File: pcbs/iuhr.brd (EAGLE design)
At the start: 38.4 x 23 mm, 81 parts, among them Q1 20.000MHz, Q2 MOSFET-NCHANNELSMD

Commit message: correct power-on button and add detection
ToDo: - reassign DIGIT6
      - layout for this commit
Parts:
- added 12V_IN1: TPTP20SQ, testpad:TP20SQ
- added D1: (no value), diode:SOD323-R
- R12: value 100 -> 14k
- moved R12 40.2 mm to (0.60, -14.4), flipped to the top, turned to 0 degrees
- renumbered ONBTN to ONBTN_B, ONBTN_3V3 to ONBTN_A
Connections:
- new net N$63: 12V_IN1.TP, R12.2
- new net N$64: ATMEGA88PA.11, D1.A
- net DIGIT6: no longer ATMEGA88PA.19
- net N$59: now also ONBTN_A.TP, R12.1; no longer ONBTN_B.TP, R12.2
- net ON: now also ATMEGA88PA.19, D1.C, ONBTN_B.TP; no longer ATMEGA88PA.11, R12.1
- net VCC: no longer ONBTN_A.TP
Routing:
- net VCC: track 69.6 -> 64.2 mm
- net N$59: track 3.52 -> 0.00 mm
- net ON: track 23.9 -> 21.8 mm
- net DIGIT6: track 4.30 -> 3.40 mm

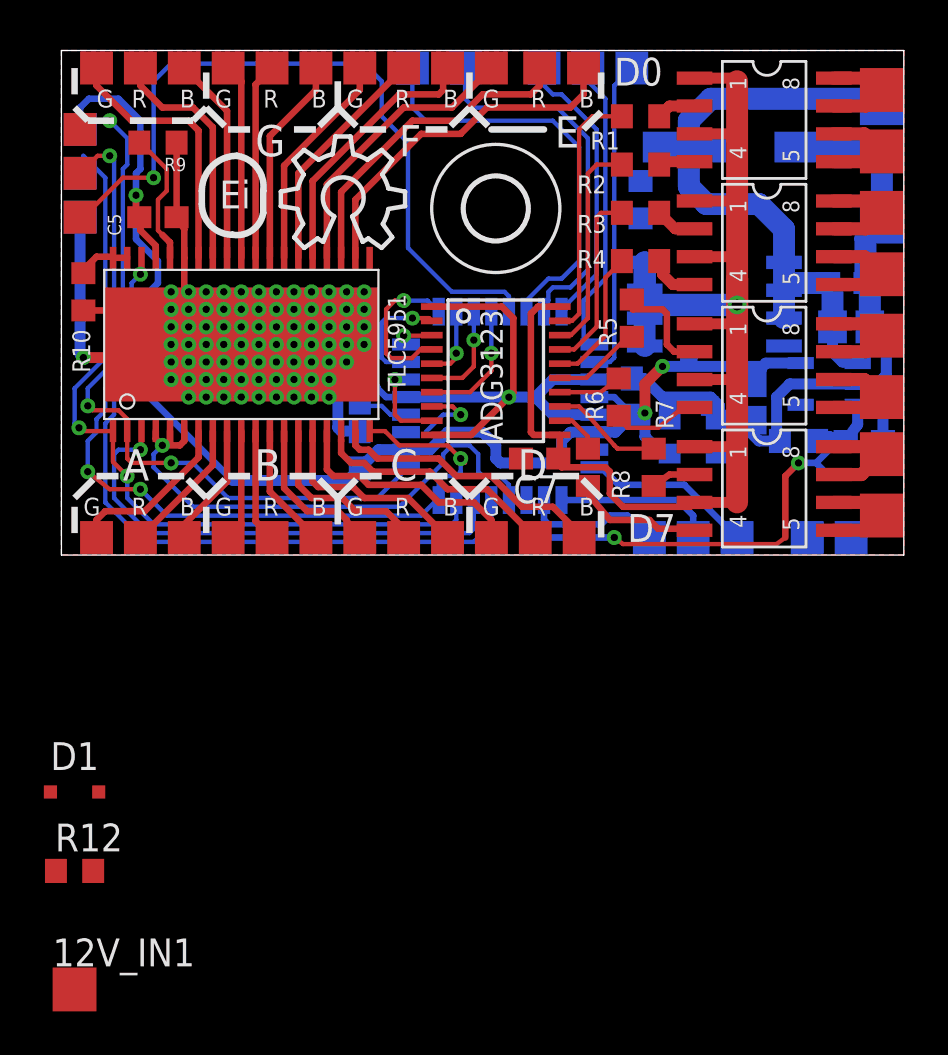
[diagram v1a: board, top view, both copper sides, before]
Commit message: Can now use "ON" Switch to turn board off
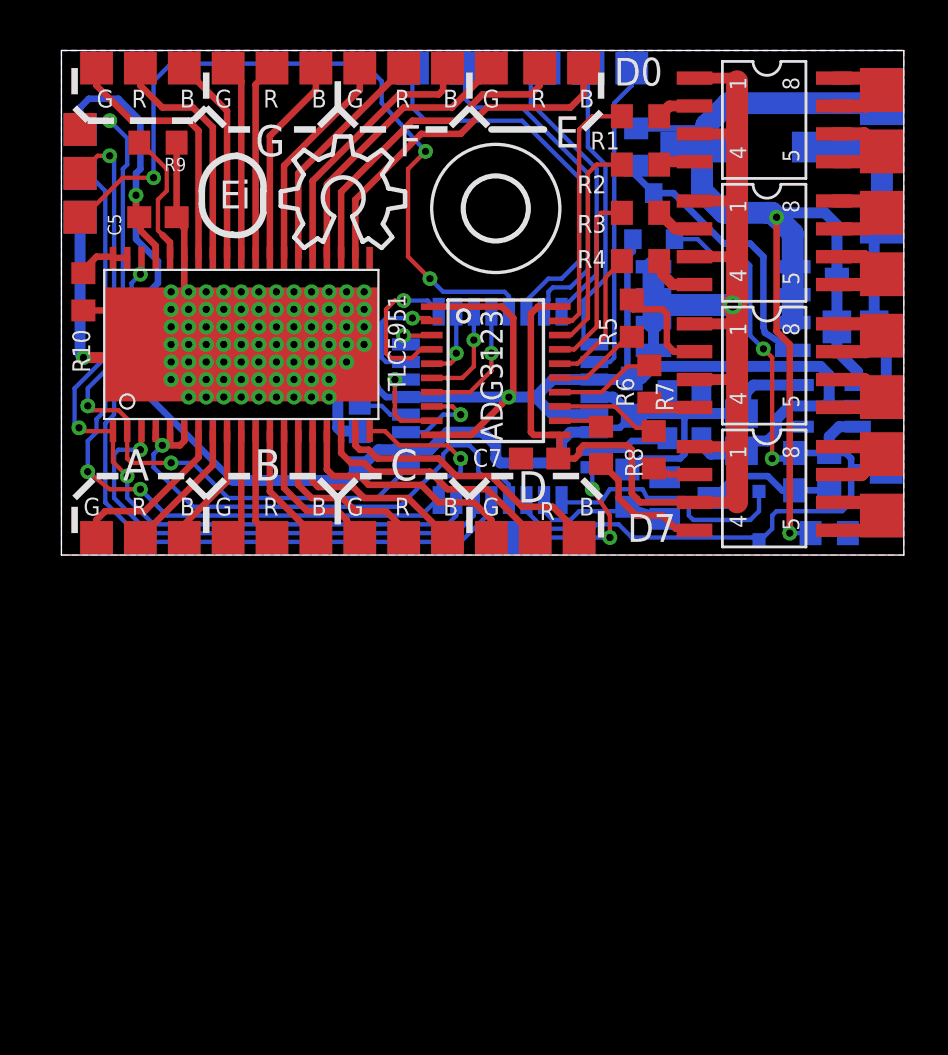
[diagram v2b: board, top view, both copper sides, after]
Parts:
- removed 12V_IN1: TPTP20SQ, testpad:TP20SQ
- removed PD5, PD6: TPTP15SQ, testpad:TP15SQ
- removed U$2: IRF7416, ShortCircuitRobotics:SO8-2
- added D2: 4.7V, diode:SOT23
- added IRF7416: IRF7416, ShortCircuitRobotics:SO8-2
- added R14: 300, resistor:R0603
- moved R12 37.7 mm to (35.0, 1.00), flipped to the bottom
- moved D1 33.6 mm to (31.8, 1.80), flipped to the bottom, turned to 90 degrees
- moved PB7 10.4 mm to (20.4, 0.80)
- moved Q2 7.77 mm to (27.0, 15.4)
- moved ONBTN_A 3.69 mm to (37.6, 1.60), turned to 270 degrees
- moved ONBTN_B 3.58 mm to (37.6, 4.00)
- moved C8 3.49 mm to (33.4, 3.80), turned to 270 degrees
- moved R13 2.41 mm to (26.2, 18.6)
- moved R11 1.98 mm to (35.0, 3.80), turned to 90 degrees
- moved R6 1.52 mm to (26.8, 7.80)
- moved C6 1.46 mm to (31.0, 5.60)
- moved R8 1.17 mm to (24.6, 5.00)
- moved Q1 1.08 mm to (28.4, 6.40), turned to 270 degrees
- moved TPS70933 1.00 mm to (35.0, 6.80)
- moved C13 0.80 mm to (32.2, 18.6)
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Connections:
- removed net N$63: 12V_IN1.TP, R12.2
- removed net N$64: ATMEGA88PA.11, D1.A
- net +12V: now also IRF7416.1, IRF7416.2, IRF7416.3, R12.2; no longer U$2.1, U$2.2, U$2.3
- net DIGIT6: now also ATMEGA88PA.19
- net GND: now also D2.3
- net N$56: now also D1.A; no longer PD5.TP
- net N$57: now also D2.1, R14.1; no longer PD6.TP
- net N$61: now also IRF7416.4; no longer U$2.4
- net ON: now also ATMEGA88PA.11; no longer ATMEGA88PA.19
- net VCC: now also R14.2
- net VPP: now also IRF7416.5, IRF7416.6, IRF7416.7, IRF7416.8; no longer U$2.5, U$2.6, U$2.7, U$2.8
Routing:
- net +12V: track 29.9 -> 50.4 mm, vias 0 -> 2
- net ON: track 21.8 -> 40.1 mm
- net GND: track 103.9 -> 119.9 mm
- net N$61: track 0.00 -> 12.8 mm
- net N$56: track 7.29 -> 12.2 mm
- net CLK_STM: track 0.00 -> 3.55 mm
- net N$44: track 4.11 -> 2.15 mm
- net N$59: track 0.00 -> 1.93 mm
- net N$46: track 2.89 -> 4.59 mm
- net MOSI: track 35.7 -> 34.4 mm
- net VCC: track 64.2 -> 65.3 mm, vias 3 -> 1
- net N$12: track 17.0 -> 16.0 mm
- net N$58: track 7.83 -> 8.76 mm, vias 0 -> 2
- net DIGIT6: track 3.40 -> 4.30 mm
- net RESET: track 34.6 -> 35.5 mm, vias 1 -> 3
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- added copper zone on layer 16, net GND

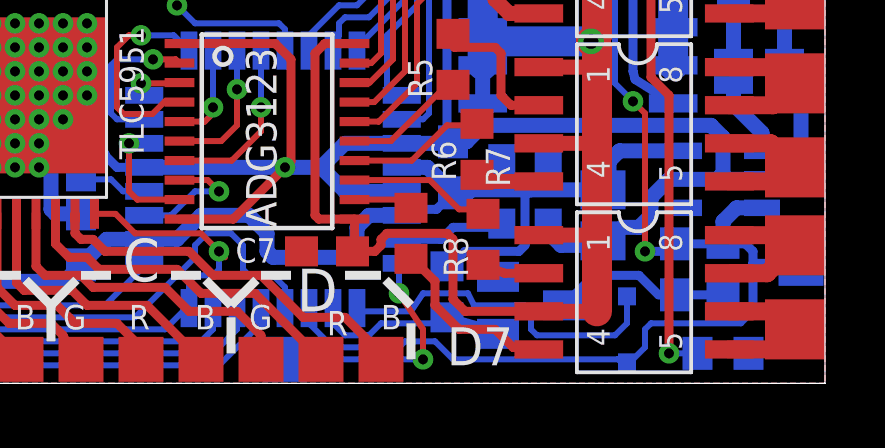
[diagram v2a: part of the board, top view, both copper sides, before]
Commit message: Swap functionality of PB7 and PD5
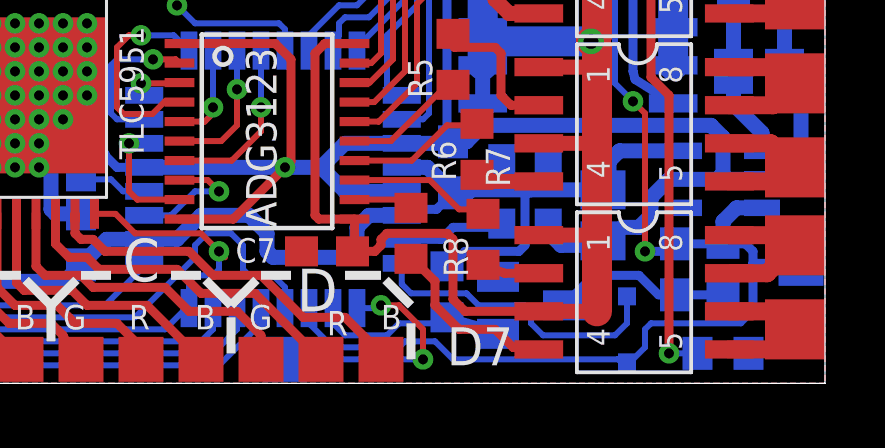
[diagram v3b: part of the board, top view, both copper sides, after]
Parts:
- renumbered PB7 to PD5
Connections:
- net N$56: now also PD5.TP; no longer D1.A
- net N$58: now also D1.A; no longer PD5.TP
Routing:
- net N$56: track 12.2 -> 8.17 mm, vias 0 -> 2
- net N$58: track 8.76 -> 10.3 mm, vias 2 -> 0
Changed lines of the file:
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@@
 <grid distance="0.2" unitdist="mm" unit="mm" style="dots" multiple="1" display="yes" altdistance="0.15875" altunitdist="mm" altunit="mm"/>
 <layers>
-<layer number="1" name="Top" color="4" fill="1" visible="no" active="yes"/>
+<layer number="1" name="Top" color="4" fill="1" visible="yes" active="yes"/>
 <layer number="2" name="Route2" color="1" fill="3" visible="no" active="no"/>
 <layer number="3" name="Route3" color="4" fill="3" visible="no" active="no"/>
@@
 <layer number="19" name="Unrouted" color="6" fill="1" visible="yes" active="yes"/>
 <layer number="20" name="Dimension" color="15" fill="1" visible="yes" active="yes"/>
-<layer number="21" name="tPlace" color="7" fill="1" visible="no" active="yes"/>
+<layer number="21" name="tPlace" color="7" fill="1" visible="yes" active="yes"/>
 <layer number="22" name="bPlace" color="7" fill="1" visible="yes" active="yes"/>
-<layer number="23" name="tOrigins" color="15" fill="1" visible="no" active="yes"/>
+<layer number="23" name="tOrigins" color="15" fill="1" visible="yes" active="yes"/>
 <layer number="24" name="bOrigins" color="15" fill="1" visible="yes" active="yes"/>
-<layer number="25" name="tNames" color="7" fill="1" visible="no" active="yes"/>
+<layer number="25" name="tNames" color="7" fill="1" visible="yes" active="yes"/>
 <layer number="26" name="bNames" color="7" fill="1" visible="yes" active="yes"/>
 <layer number="27" name="tValues" color="7" fill="1" visible="no" active="yes"/>
@@
 <layer number="37" name="tTest" color="7" fill="1" visible="no" active="yes"/>
 <layer number="38" name="bTest" color="7" fill="1" visible="no" active="yes"/>
-<layer number="39" name="tKeepout" color="4" fill="11" visible="no" active="yes"/>
+<layer number="39" name="tKeepout" color="4" fill="11" visible="yes" active="yes"/>
 <layer number="40" name="bKeepout" color="1" fill="11" visible="yes" active="yes"/>
 <layer number="41" name="tRestrict" color="4" fill="10" visible="no" active="yes"/>
@@
 <layer number="49" name="Reference" color="7" fill="1" visible="no" active="yes"/>
 <layer number="50" name="dxf" color="7" fill="1" visible="no" active="no"/>
-<layer number="51" name="tDocu" color="7" fill="1" visible="no" active="yes"/>
+<layer number="51" name="tDocu" color="7" fill="1" visible="yes" active="yes"/>
 <layer number="52" name="bDocu" color="7" fill="1" visible="yes" active="yes"/>
 <layer number="53" name="tGND_GNDA" color="7" fill="9" visible="no" active="no"/>
@@
 <element name="H2" library="holes" package="2,8" value="MOUNT-HOLE2.8" x="19.8" y="15.8"/>
 <element name="LOGO1" library="ea" package="OSHW_8X200_NOTEXT" value="OSHW_LOGO_8MILX0200-NT" x="10" y="14"/>
-<element name="PB7" library="testpad" package="TP15SQ" value="TPTP15SQ" x="20.4" y="0.8" smashed="yes" rot="MR0">
+<element name="PD5" library="testpad" package="TP15SQ" value="TPTP15SQ" x="20.4" y="0.8" smashed="yes" rot="MR0">
 <attribute name="TP_SIGNAL_NAME" value="" x="20.4" y="-1.74" size="1" layer="38" rot="MR0"/>
 <attribute name="NAME" x="20.7501" y="4.0001" size="0.8128" layer="26" rot="MR270"/>
@@
 <signal name="N$58">
 <contactref element="ATMEGA88PA" pad="8"/>
-<contactref element="PB7" pad="TP"/>
-<wire x1="20.4" y1="0.8" x2="20.8" y2="0.8" width="0.2" layer="16"/>
-<wire x1="20.8" y1="0.8" x2="21" y2="0.6" width="0.2" layer="16"/>
-<via x="25" y="0.8" extent="1-16" drill="0.3302"/>
-<wire x1="25" y1="0.8" x2="25" y2="1.8" width="0.2" layer="1"/>
-<wire x1="25" y1="1.8" x2="24.2" y2="3" width="0.2" layer="1"/>
-<via x="24.2" y="3" extent="1-16" drill="0.3302"/>
-<wire x1="24.2" y1="3" x2="24.2" y2="3.9074" width="0.2" layer="16"/>
 <wire x1="24.2" y1="3.9074" x2="24.2926" y2="4" width="0.2" layer="16"/>
-<wire x1="25" y1="0.8" x2="20.4" y2="0.8" width="0.2" layer="16"/>
+<contactref element="D1" pad="A"/>
+<wire x1="24.2926" y1="4" x2="24.2926" y2="3.3074" width="0.2" layer="16"/>
+<wire x1="24.2926" y1="3.3074" x2="24.6" y2="3" width="0.2" layer="16"/>
+<wire x1="24.6" y1="3" x2="26.45" y2="3" width="0.2" layer="16"/>
+<wire x1="26.45" y1="3" x2="26.85" y2="2.6" width="0.2" layer="16"/>
+<wire x1="26.85" y1="2.6" x2="28.4" y2="2.6" width="0.2" layer="16"/>
+<wire x1="28.4" y1="2.6" x2="28.6" y2="2.4" width="0.2" layer="16"/>
+<wire x1="28.6" y1="2.4" x2="28.6" y2="2" width="0.2" layer="16"/>
+<wire x1="28.6" y1="2" x2="29" y2="1.6" width="0.2" layer="16"/>
+<wire x1="29" y1="1.6" x2="31.4" y2="1.6" width="0.2" layer="16"/>
+<wire x1="31.4" y1="1.6" x2="31.8" y2="2" width="0.2" layer="16"/>
+<wire x1="31.8" y1="2" x2="31.8" y2="2.9" width="0.2" layer="16"/>
 </signal>
 <signal name="VPP">
@@
 <wire x1="37.2" y1="1.2" x2="37.6" y2="1.6" width="0.3" layer="16"/>
 </signal>
-<signal name="N$56">
-<contactref element="ATMEGA88PA" pad="9"/>
-<contactref element="D1" pad="A"/>
-<wire x1="28.4" y1="2.6" x2="28.6" y2="2.4" width="0.2" layer="16"/>
-<wire x1="28.6" y1="2.4" x2="28.6" y2="1.8" width="0.2" layer="16"/>
-<wire x1="28.6" y1="1.8" x2="28.8" y2="1.6" width="0.2" layer="16"/>
-<wire x1="28.8" y1="1.6" x2="31.4" y2="1.6" width="0.2" layer="16"/>
-<wire x1="31.4" y1="1.6" x2="31.8" y2="2" width="0.2" layer="16"/>
-<wire x1="31.8" y1="2" x2="31.8" y2="2.9" width="0.2" layer="16"/>
-<wire x1="22.8926" y1="2.6" x2="22.8926" y2="2.3074" width="0.2" layer="16"/>
-<wire x1="22.8" y1="2.5074" x2="22.8926" y2="2.6" width="0.3" layer="16"/>
-<wire x1="25" y1="3" x2="26.5" y2="3" width="0.2" layer="16"/>
-<wire x1="26.7" y1="2.6" x2="28.4" y2="2.6" width="0.2" layer="16"/>
-<wire x1="22.8926" y1="2.1074" x2="22.8926" y2="2.3074" width="0.2" layer="16"/>
-<wire x1="22.8926" y1="2.3074" x2="22.8" y2="2.4" width="0.2" layer="16"/>
-<wire x1="22.8" y1="2.4" x2="24.6" y2="2.4" width="0.2" layer="16"/>
-<wire x1="24.6" y1="2.4" x2="25" y2="3" width="0.2" layer="16"/>
-<wire x1="26.5" y1="3" x2="26.7" y2="2.6" width="0.2" layer="16"/>
-</signal>
 <signal name="N$57">
 <contactref element="D2" pad="1"/>
@@
 <wire x1="25.8" y1="2.2" x2="27.4" y2="1.75" width="0.3" layer="16"/>
 <wire x1="27.4" y1="1.75" x2="27.5" y2="1.65" width="0.3" layer="16"/>
-<wire x1="22.4" y1="1.6" x2="23.2" y2="1.6" width="0.2" layer="16"/>
-<wire x1="23.2" y1="1.6" x2="23.6" y2="2" width="0.2" layer="16"/>
-<wire x1="23.6" y1="2" x2="25.65" y2="2" width="0.2" layer="16"/>
+<wire x1="22.4" y1="1.6" x2="23.8" y2="1.6" width="0.2" layer="16"/>
+<wire x1="23.8" y1="1.6" x2="24.2" y2="2" width="0.2" layer="16"/>
+<wire x1="24.2" y1="2" x2="25.65" y2="2" width="0.2" layer="16"/>
 <wire x1="25.65" y1="2" x2="25.8" y2="2.2" width="0.2" layer="16"/>
 </signal>
+<signal name="N$56">
+<contactref element="ATMEGA88PA" pad="9"/>
+<contactref element="PD5" pad="TP"/>
+<wire x1="20.4" y1="0.8" x2="25" y2="0.8" width="0.2" layer="16"/>
+<wire x1="25" y1="0.8" x2="25" y2="1.8" width="0.2" layer="1"/>
+<wire x1="25" y1="1.8" x2="24.2" y2="2.6" width="0.2" layer="1"/>
+<wire x1="24.2" y1="2.6" x2="23.6" y2="2.6" width="0.2" layer="1"/>
+<wire x1="23.6" y1="2.6" x2="23.5074" y2="2.5074" width="0.2" layer="16"/>
+<wire x1="23.5074" y1="2.5074" x2="22.8" y2="2.5074" width="0.2" layer="16"/>
+<via x="23.6" y="2.6" extent="1-16" drill="0.332"/>
+<via x="25" y="0.8" extent="1-16" drill="0.332"/>
+</signal>
 </signals>

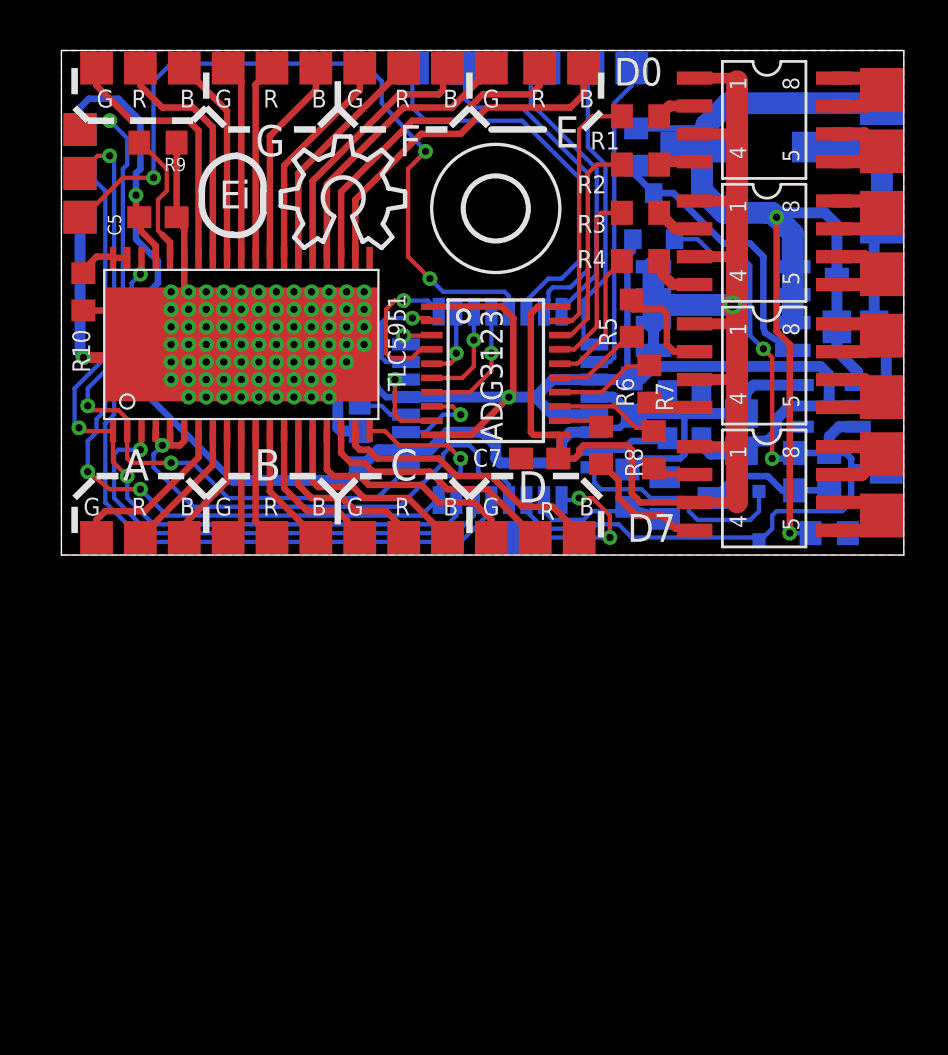
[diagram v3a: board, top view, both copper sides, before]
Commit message: Improved GND connectivity
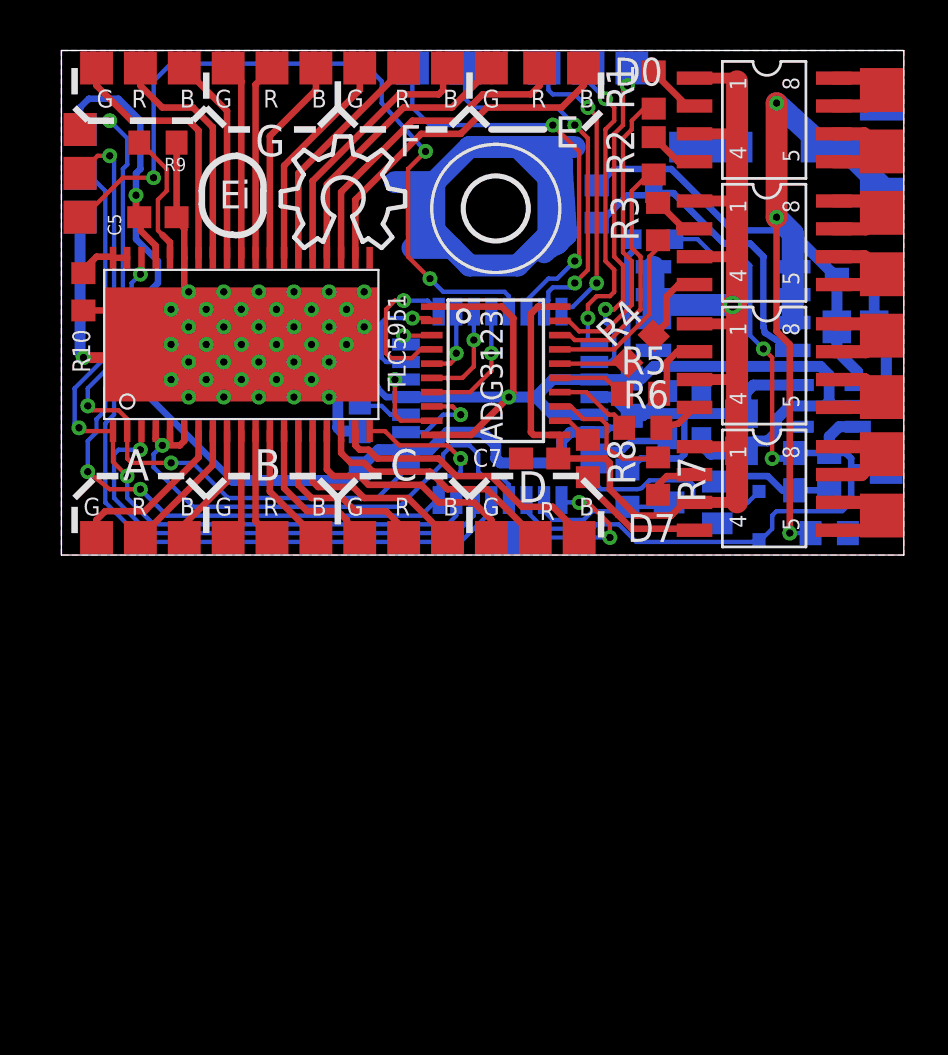
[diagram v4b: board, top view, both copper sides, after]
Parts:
- moved GND_IN 5.60 mm to (37.4, 20.8)
- moved 12V_IN 4.40 mm to (37.4, 16.2)
- moved R4 4.00 mm to (26.4, 9.40), turned to 45 degrees
- moved R5 3.47 mm to (26.4, 7.35), turned to 0 degrees
- moved R13 3.16 mm to (24.4, 16.0)
- moved R6 2.02 mm to (26.5, 5.80), turned to 0 degrees
- moved R1 1.34 mm to (27.0, 21.2), turned to 90 degrees
- moved R7 1.22 mm to (27.2, 3.60)
- moved R3 0.89 mm to (27.2, 15.2), turned to 90 degrees
- moved R8 0.85 mm to (24.0, 4.40)
- moved R2 0.72 mm to (27.0, 18.2), turned to 90 degrees
- moved C13 0.40 mm to (32.6, 18.6), turned to 180 degrees
- moved D2 0.28 mm to (28.8, 2.40), turned to 270 degrees
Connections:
- net GND: now also D2.1; no longer D2.3
- net N$57: now also D2.3; no longer D2.1
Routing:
- net GND: track 119.9 -> 149.0 mm, vias 80 -> 41
- net N$40: track 6.32 -> 3.11 mm
- net N$33: track 11.6 -> 13.9 mm
- net N$43: track 4.88 -> 3.00 mm
- net N$21: track 13.3 -> 15.0 mm, vias 0 -> 2
- net N$61: track 12.8 -> 14.3 mm
- net N$51: track 4.75 -> 6.07 mm
- net N$47: track 9.92 -> 11.2 mm
- net N$38: track 2.32 -> 3.53 mm
- net N$53: track 13.8 -> 14.9 mm, vias 0 -> 2
- net +12V: track 50.4 -> 51.4 mm, vias 2 -> 3
- net N$45: track 4.06 -> 3.12 mm
- net N$12: track 16.0 -> 17.0 mm, vias 0 -> 2
- net N$46: track 4.59 -> 3.68 mm
- net N$54: track 14.5 -> 15.4 mm, vias 0 -> 2
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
